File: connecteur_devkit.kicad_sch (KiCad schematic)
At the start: 8 parts, among them J10 OLED_SPI_2x8, J17 DEVKIT_C2000_A, J18 DEVKIT_C2000_B, J7 ESP32_C6_DEVKITC_1_J1, J8 ESP32_C6_DEVKITC_1_J3, U4 ER-OLEDM032-1

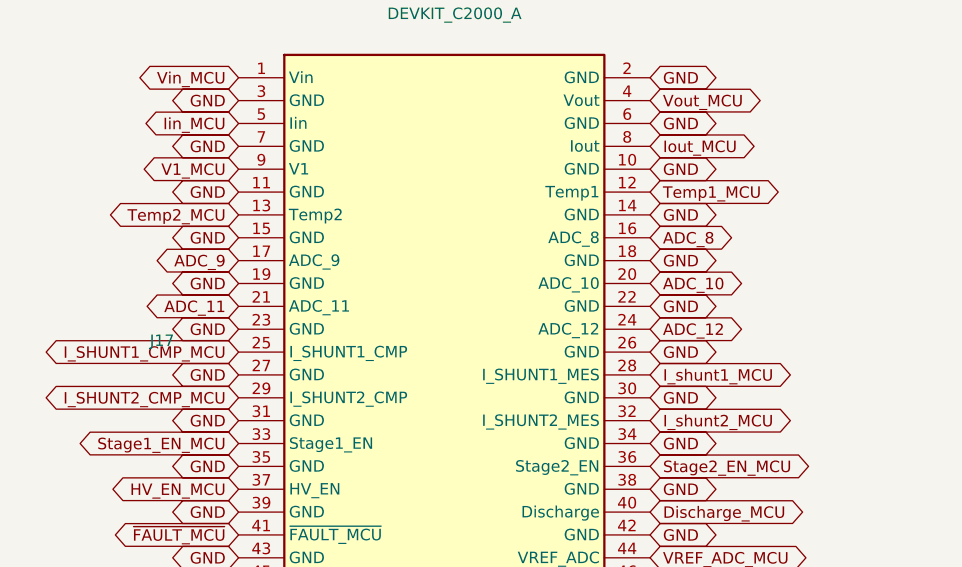
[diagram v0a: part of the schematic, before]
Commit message: Ajoute les connecteurs dedies carte HV et carte Filament (HT)
Ecart assume a la decision #17 : ces deux premieres cartes filles ont
plus de signaux que les reserves des six nappes partagees n'en offrent
(ADC-2: 3 reserves, GPIO-1: aucune). Chaque carte recoit son propre
connecteur IDC 2x10 sur une feuille dediee, en plus des six nappes.

- connecteur_carte_hv.kicad_sch (J19/J20) : tous les signaux repris
  sont deja proteges ailleurs, aucun composant neuf.
- connecteur_ht.kicad_sch (J21) : les 5 voies ADC_8-12 du devkit,
  posees depuis le debut mais jamais cablees, sont enfin affectees
  (Vht/Temp_ht/I_Shunt_ht/I_Shunt_ht_comp/V_bias) via 5 nouveaux trios
  de protection (gabarit existant, R=22 Ohm sur le chemin comparateur
  I_Shunt_ht_comp/CMPSS3, R=100 Ohm ailleurs).
- 3 nouveaux symboles NAPPE_HV_ADC/NAPPE_HV_DIO/NAPPE_FILAMENT_HT
  (gabarit NAPPE_ADC1).
- Renommage prealable des labels ADC_8-12 en _MCU sur
  connecteur_devkit.kicad_sch (convention stricte du projet).

Verifie : check_schematic_labels.py propre sur les 3 feuilles ; ERC
feuille par feuille/categorie contre l'etat precedent, 0 violation sur
les deux nouvelles feuilles, les 5 isolated_pin_label sur ADC_8-12 ont
disparu, aucune regression ailleurs.

Hors perimetre : PCB non touche ; configuration CMPSS3 cote firmware
devkit (projet CCS separe) a faire plus tard.

Co-Authored-By: Claude Sonnet 5 <noreply@anthropic.com>
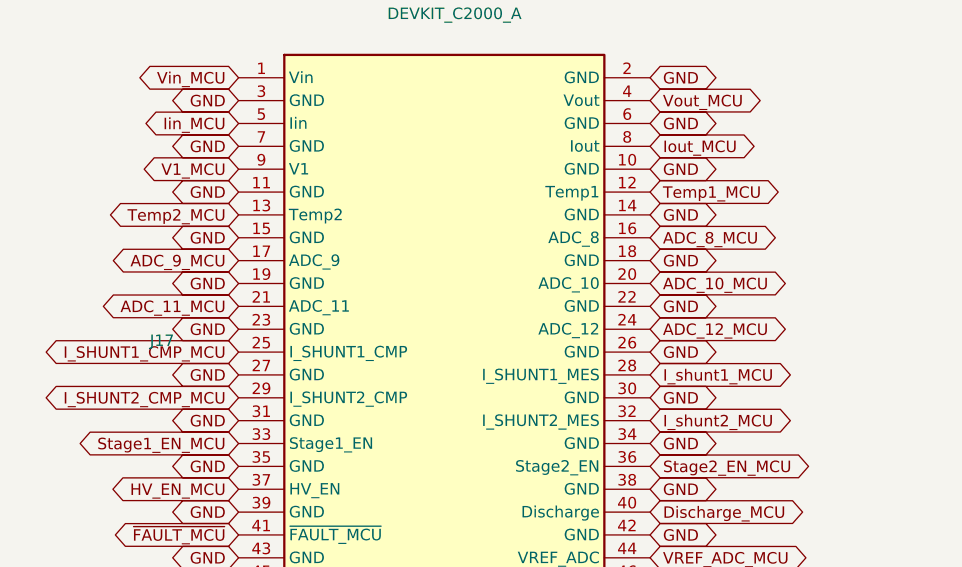
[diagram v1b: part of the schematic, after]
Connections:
- net ADC_10 renamed ADC_10_MCU
- net ADC_11 renamed ADC_11_MCU
- net ADC_12 renamed ADC_12_MCU
- net ADC_8 renamed ADC_8_MCU
- net ADC_9 renamed ADC_9_MCU
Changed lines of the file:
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@@
 		)
 	)
-	(global_label "ADC_8"
+	(global_label "ADC_8_MCU"
 		(shape bidirectional)
 		(at 90.932 47.244 0)
@@
 		)
 	)
-	(global_label "ADC_9"
+	(global_label "ADC_9_MCU"
 		(shape bidirectional)
 		(at 45.212 49.784 180)
@@
 		)
 	)
-	(global_label "ADC_10"
+	(global_label "ADC_10_MCU"
 		(shape bidirectional)
 		(at 90.932 52.324 0)
@@
 		)
 	)
-	(global_label "ADC_11"
+	(global_label "ADC_11_MCU"
 		(shape bidirectional)
 		(at 45.212 54.864 180)
@@
 		)
 	)
-	(global_label "ADC_12"
+	(global_label "ADC_12_MCU"
 		(shape bidirectional)
 		(at 90.932 57.404 0)

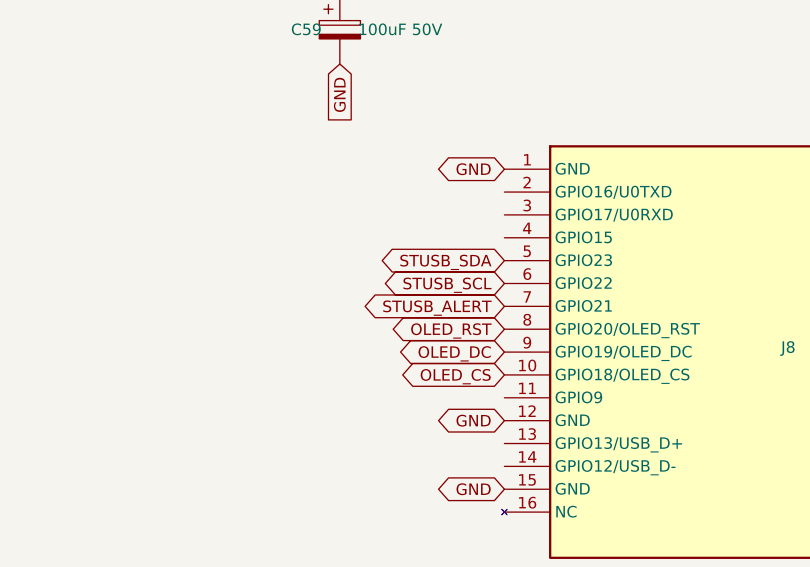
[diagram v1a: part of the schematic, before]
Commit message: Isole la liaison ESP32<->STUSB4531 (ISO1640BD + DPC817), USB-PD rejoint GND_PRI
Le bus de supervision I2C/ALERT (STUSB_SCL/STUSB_SDA/STUSB_ALERT) reliait
directement GPIO22/23/21 aux pins de U1, sans isolation. Isole avec :
- ISO1640BD (TI, 8-SOIC, isolation basique 3000VRMS) pour SCL/SDA -
  symbole dessine a la main (absent des bibliotheques stock), empreinte
  SOIC-8 standard.
- DPC817 (optocoupleur, NRND mais empreinte generique standard 4 broches)
  pour ALERT - brochage repris du symbole stock PC817, empreinte SL-4
  dessinee a la main (aucune empreinte stock ne correspondait).

Reutilise les pull-ups existants R45/R46/R47 (4,7k vers 3V3_ESP32) comme
cote Side 1 de l'isolateur, simplement renommes (ESP32_SCL_ISO/
ESP32_SDA_ISO/ESP32_ALERT_ISO). VREG_2V7 (deja existant) alimente le
Side 2, avec 2 pull-ups neufs (2,2k) + 1 resistance limiteuse LED (330R).

Clarification plus large de l'utilisateur : tout usb_pd.kicad_sch (16
occurrences de GND, pas seulement l'isolateur) rejoint GND_PRI - le
sous-systeme USB-PD (20V) appartient au meme domaine primaire que le
connecteur 11-25V, separe de GND par les convertisseurs 3,3V existants.
GND_PRI etait deja classe Isole_Primaire dans shield.kicad_pro, aucune
nouvelle regle necessaire.

Caracterise les deux composants dans composants-datasheets/ (nouvelle
famille isolator_digital, lint propre).

Bug trouve en implementant : (shape power_in) est un mot-cle invalide
pour global_label, fait echouer la connexion ERC silencieusement -
documente en decision #27 pour ne pas le reproduire.

Verifie : ERC feuille par feuille/categorie contre l'etat precedent,
aucune regression (le seul power_pin_not_driven neuf sur GND_PRI/U5 est
attendu, meme caracteristique deja acceptee que VIN_PWR/GND_PRI sur DC).

Co-Authored-By: Claude Sonnet 5 <noreply@anthropic.com>
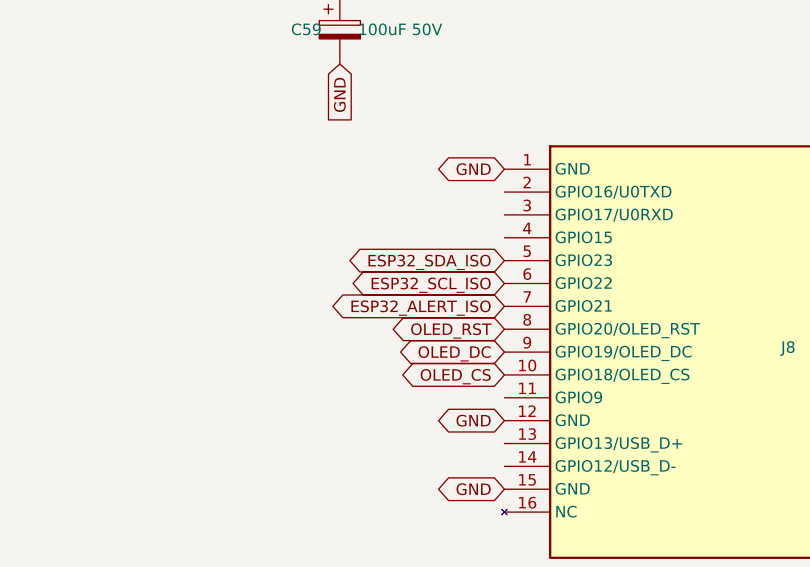
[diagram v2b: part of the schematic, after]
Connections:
- net STUSB_ALERT renamed ESP32_ALERT_ISO
- net STUSB_SCL renamed ESP32_SCL_ISO
- net STUSB_SDA renamed ESP32_SDA_ISO
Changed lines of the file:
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@@
 		)
 	)
-	(global_label "STUSB_ALERT"
+	(global_label "ESP32_ALERT_ISO"
 		(shape bidirectional)
 		(at 358.14 113.792 180)
@@
 		)
 	)
-	(global_label "STUSB_SDA"
+	(global_label "ESP32_SDA_ISO"
 		(shape bidirectional)
 		(at 358.14 108.712 180)
@@
 		)
 	)
-	(global_label "STUSB_SCL"
+	(global_label "ESP32_SCL_ISO"
 		(shape bidirectional)
 		(at 358.14 111.252 180)
